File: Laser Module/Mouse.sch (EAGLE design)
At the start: 74 parts, among them Q2 2.5A/30V, U1 RFM69HCW, U10 74AHC1G125, U2 HALL-EFFECTSMD, U3 HALL-EFFECTSMD, U4 HALL-EFFECTSMD, U5 HALL-EFFECTSMD, U6 BQ27441-G1, U7 BQ24075, U8 ATSAMD21G-A, U9 3.3V, Y1 32.768kHz

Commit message: Worked on the laser and dongle schematics Placed the parts on the laser and dongle boards in their rough locations
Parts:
- removed D7: RED, SparkFun-LED:LED-RED0603
- removed F1: 500mA, SparkFun-PowerIC:PTCSMD
- removed L1: FB - 30Ohm, SparkFun-Passives:INDUCTOR0603
- removed Q2: 2.5A/30V, SparkFun-DiscreteSemi:MOSFET-PCHANNELDMG2307L
- removed R19: 10K, SparkFun-Resistors:10KOHM-1/10W-1%(0603)0603
- removed R32: 47K, SparkFun-Resistors:47KOHM1/10W1%(0603)
- removed SJ6: PWR-LED, SparkFun-Passives:JUMPER-PAD-2-NC_BY_TRACENO_SILK
- removed U10: 74AHC1G125, SparkFun-DigitalIC:74AHC1G125
- added ANT: (no value), SparkFun-Connectors:M01PTH_2MM
- added LASER: (no value), SparkFun-Connectors:M021X02_NO_SILK
- added Q1: MOSFET-NCHANNELAO3404A, SparkFun-DiscreteSemi:MOSFET-NCHANNELAO3404A
- added R10, R20, R21, R23, R25, R29: 10k, SparkFun-Resistors:330OHM1/10W1%(0603)
- added R33: 10K, SparkFun-Resistors:10KOHM-1/10W-1%(0603)0603
- added S3, S5, S6, S7, S8, S9: SWITCH-MOMENTARY-2SMD-4, SparkFun-Electromechanical:SWITCH-MOMENTARY-2SMD-4
- JP22: value CORTEX_DEBUGPTH -> CORTEX_DEBUGSMD; device samd21-temp:CORTEX_DEBUGPTH -> SparkFun-Connectors:CORTEX_DEBUGSMD
- R18: value 10K -> 330; device SparkFun-Resistors:10KOHM-1/10W-1%(0603)0603 -> SparkFun-Resistors:330OHM1/10W1%(0603)
- R28: value 330 -> 10k
- S4: value RESET -> SWITCH-MOMENTARY-2SMD-4; device samd21-temp:SWITCH-MOMENTARY-2SMD-4.6X2.8MM -> SparkFun-Electromechanical:SWITCH-MOMENTARY-2SMD-4
- renumbered JP11 to SUPP
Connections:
- removed net A0: U8.PA02(AIN0/DAC)
- removed net A1: U8.PB08(AIN2/SER4:0/TC4:0)
- removed net A2: U8.PB09(AIN3/SER4:1/TC4:1)
- removed net A3: U8.PA04(AIN4/REFB/SER0:0/TC0:0)
- removed net AREF: U8.PA03(AIN1/REFA)
- removed net D0/RXI: U8.PA11(AIN19/SER0:3+)
- removed net D1/TXO: U8.PA10(AIN18/SER0:2+)
- removed net D10/SS: U8.PA18(SER1:2+)
- removed net D11/MOSI: U8.PA16(I2C/SER1:0+)
- removed net D12/MISO: U8.PA19(SER1:3+)
- removed net D13/SCK: U8.PA17(I2C/SER1:1+)
- removed net D2: U8.PA14(XIN/SER2:2+)
- removed net D3: U8.PA09(I2C/AIN17/SER0:1+)
- removed net D4: U8.PA08(I2C/AIN16/SER0:0+)
- removed net D5: U8.PA15(XOUT/SER2:3+)
- removed net D6: U8.PA20(SER5:2+)
- removed net D7: U8.PA21(SER5:3+)
- removed net D8: U8.PA06(AIN6/SER0:2/TC1:0)
- removed net D9: U8.PA07(AIN7/SER0:3/TC1:1)
- removed net EN2: U7.EN2
- removed net N$14: D7.A, R28.1
- removed net N$18: F1.2, Q2.D
- removed net N$20: Q2.G, R32.1, U10.Y
- removed net N$23: D7.C, SJ6.2
- removed net RF_NSS: U1.NSS
- removed net RX_LED: U8.PB03(AIN11/SER5:1)
- removed net SCL: U8.PA23(I2C/SER3:0+)
- removed net SDA: U8.PA22(I2C/SER3:0+)
- removed net TRK_BTN: R5.2, S1.2
- removed net TX_LED: U8.PA27
- new net DWN_BTN: R23.2, S6.1, U8.PA10(AIN18/SER0:2+)
- new net LFT_BTN: R10.2, S3.1, U8.PB09(AIN3/SER4:1/TC4:1)
- new net LFT_MOUSE: R28.2, S8.1, U8.PA12(I2C/SER2:0+)
- new net LSR_BTN: R25.2, S7.1, U8.PA11(AIN19/SER0:3+)
- new net LSR_OUT: R18.2, U8.PA04(AIN4/REFB/SER0:0/TC0:0)
- new net MDL_MOUSE: R5.2, S1.2, U8.PA06(AIN6/SER0:2/TC1:0)
- new net N$6: Q1.G, R18.1
- new net N$8: LASER.2, Q1.D
- new net RF_SS: U1.NSS, U8.PA18(SER1:2+)
- new net RHT_BTN: R21.2, S5.1, U8.PA09(I2C/AIN17/SER0:1+)
- new net RHT_MOUSE: R29.2, S9.1, U8.PA13(I2C/SER2:1+)
- new net UP_BTN: R20.2, S4.1, U8.PA08(I2C/AIN16/SER0:0+)
- net !RESET: no longer S4.2
- net 3.3V: now also S3.2, S4.2, S5.2, S6.2, S7.2, S8.2, S9.2; no longer L1.1, R28.2
- net ANT: now also ANT.1
- net BLU_PWM: now also U8.PA14(XIN/SER2:2+)
- net BMS_SCL: now also U8.PA23(I2C/SER3:0+)
- net BMS_SDA: now also U8.PA22(I2C/SER3:0+)
- net EN1: now also R33.2; no longer R18.2
- net GND: now also Q1.S, R10.1, R20.1, R21.1, R23.1, R25.1, R28.1, R29.1, U7.EN2; no longer R19.2, S4.1, SJ6.1, U10.GND
- net GPOUT: now also U8.PA05(AIN5/SER0:1/TC0:1)
- net GRN_PWM: now also U8.PA20(SER5:2+)
- net HALL_DWN: now also U8.PB02(AIN10/SER5:0)
- net HALL_LFT: now also U8.PB03(AIN11/SER5:1)
- net HALL_RHT: now also U8.PB08(AIN2/SER4:0/TC4:0)
- net HALL_UP: now also U8.PA07(AIN7/SER0:3/TC1:1)
- net N$19: no longer U10./OE, U10.A
- net OUT: now also R33.1; no longer R18.1, R19.1
- net RED_PWM: now also U8.PA15(XOUT/SER2:3+)
- net RF_MISO: now also U8.PA19(SER1:3+)
- net RF_MOSI: now also U8.PA16(I2C/SER1:0+)
- net RF_SCK: now also U8.PA17(I2C/SER1:1+)
- net VDDANA: no longer L1.2
- net VIN: no longer Q2.S, R32.2, U10.VCC
- net V_BATT: now also LASER.1
- net V_USB: no longer F1.1
- net WHT_PWM: now also U8.PA21(SER5:3+)
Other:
- note added: "Buttons"
- note added: "Laser Output"
- note removed: "Charge Current Select"
- note removed: "LEDs!!!"
- note removed: "PA12 is SPI MISO (on SPI header)."
- note removed: "PA13 is DGI GPIO0 (goes to EDBG)."
- note removed: "PA5 is A4"
- note removed: "PB10/11 are MOSI/SCK to SPI header."
- note removed: "PB2 is A5"
- note removed: "PB22/23 are TXD/RXD to the EDBG"
- note removed: "SJ1 enable's disconnecting the Power LED indicator. For power-saving requirements. Default: closed."
- moved on the sheet: C9, D5, D6, JP22, R15, R16, R18, R28, S4

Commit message: Created, placed, and routed a starter board for the Camera Module
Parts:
- ANT: device SparkFun-Connectors:M01PTH_2MM -> SparkFun-Connectors:M01PTH_NO_SILK_YES_STOP
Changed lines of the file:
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@@
 <part name="GND34" library="SparkFun-Aesthetics" deviceset="GND" device=""/>
 <part name="R33" library="SparkFun-Resistors" deviceset="10KOHM-1/10W-1%(0603)" device="0603" value="10K"/>
-<part name="ANT" library="SparkFun-Connectors" deviceset="M01" device="PTH_2MM"/>
+<part name="ANT" library="SparkFun-Connectors" deviceset="M01" device="PTH_NO_SILK_YES_STOP"/>
 <part name="Q1" library="SparkFun-DiscreteSemi" deviceset="MOSFET-NCHANNEL" device="AO3404A"/>
 <part name="GND35" library="SparkFun" deviceset="GND" device=""/>

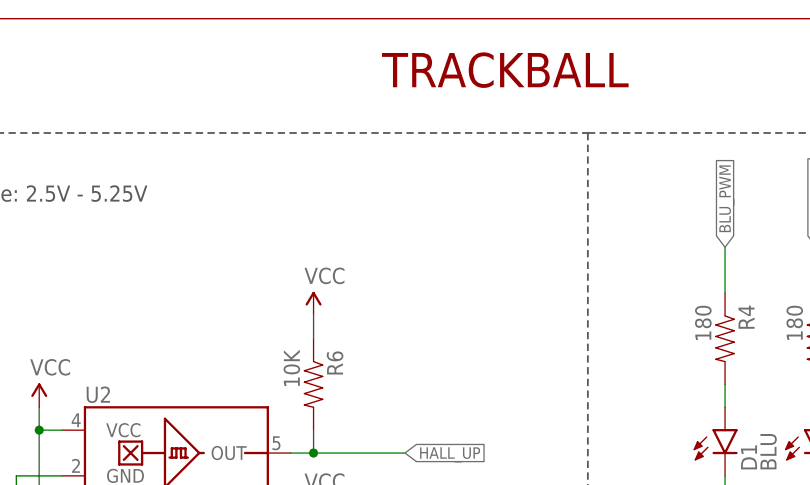
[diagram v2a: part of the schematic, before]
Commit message: Routed the dongle and camera modules
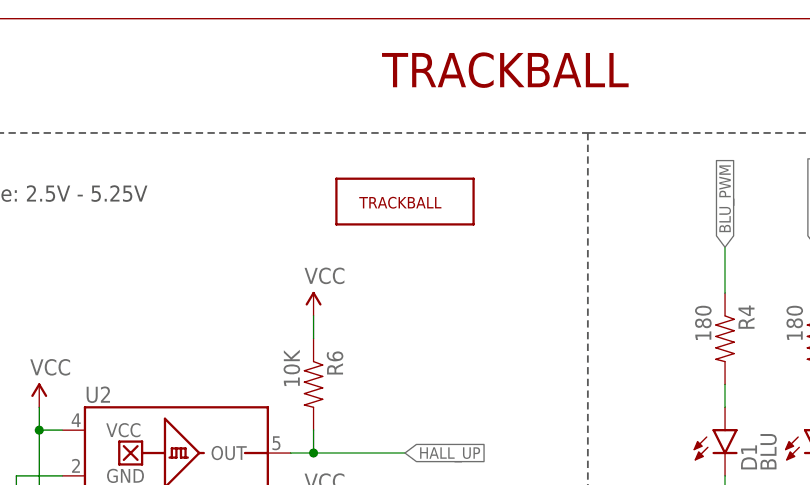
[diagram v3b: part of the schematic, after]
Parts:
- added U$1: TRACKBALLMECH, SparkFun-Electromechanical:TRACKBALLMECH
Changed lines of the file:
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@@
 <part name="LASER" library="SparkFun-Connectors" deviceset="M02" device="1X02_NO_SILK"/>
 <part name="SUPPLY23" library="SparkFun-Aesthetics" deviceset="V_BATT" device=""/>
+<part name="U$1" library="SparkFun-Electromechanical" deviceset="TRACKBALL" device="MECH"/>
 </parts>
 <sheets>
@@
 <instance part="LASER" gate="G$1" x="426.72" y="208.28" rot="R180"/>
 <instance part="SUPPLY23" gate="G$1" x="414.02" y="213.36"/>
+<instance part="U$1" gate="G$1" x="264.16" y="307.34"/>
 </instances>
 <busses>

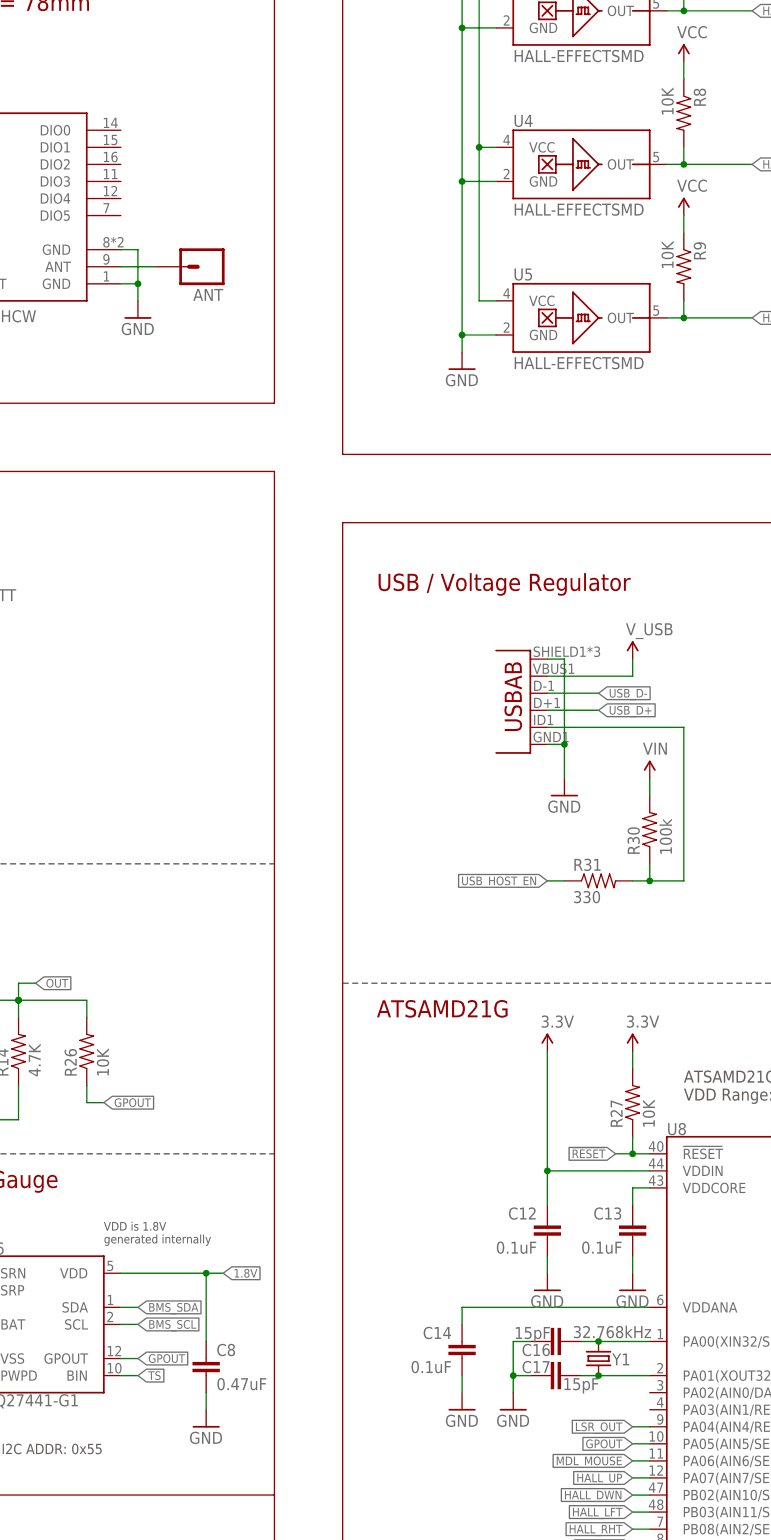
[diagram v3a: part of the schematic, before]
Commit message: Updated the RFM69 library to be closer to C. millis() is the only function hat needs to be updated now.
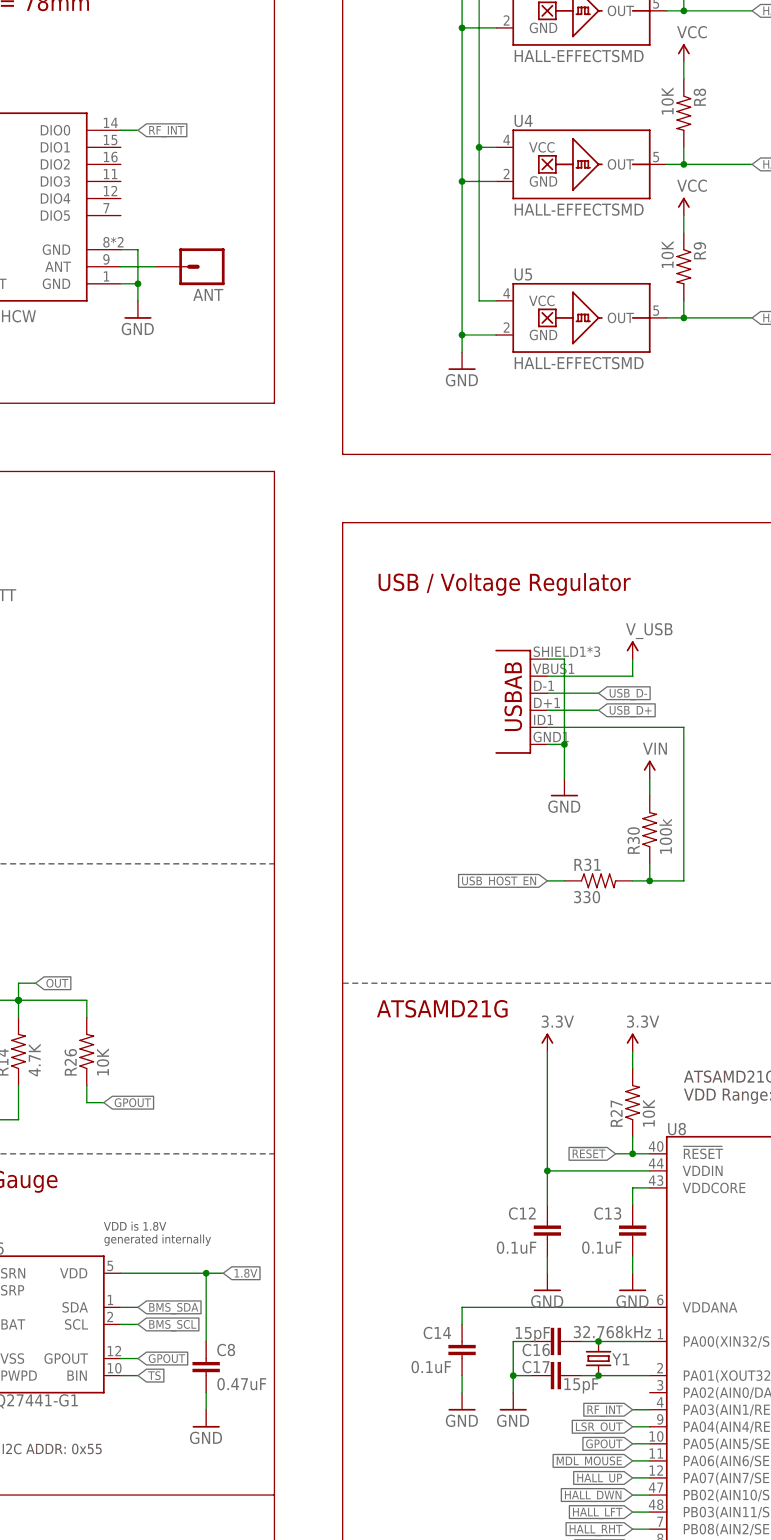
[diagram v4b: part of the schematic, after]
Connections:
- new net RF_INT: U1.DIO0, U8.PA03(AIN1/REFA)
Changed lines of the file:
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@@
+</segment>
+</net>
+<net name="RF_INT" class="0">
+<segment>
+<pinref part="U1" gate="G$1" pin="DIO0"/>
+<wire x1="170.18" y1="238.76" x2="172.72" y2="238.76" width="0.1524" layer="91"/>
+<label x="172.72" y="238.76" size="1.27" layer="95" xref="yes"/>
+</segment>
+<segment>
+<pinref part="U8" gate="G$1" pin="PA03(AIN1/REFA)"/>
+<wire x1="248.92" y1="48.26" x2="246.38" y2="48.26" width="0.1524" layer="91"/>
+<label x="246.38" y="48.26" size="1.27" layer="95" rot="R180" xref="yes"/>
 </segment>
 </net>

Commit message: Started the routing of the laser module board Updated the Dongle Module C project to allow for absolute mouse control
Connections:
- removed net VCC: C3.1, C4.1, C5.1, C6.1, R5.1, R6.1, R7.1, R8.1, R9.1, U2.VCC, U3.VCC, U4.VCC, U5.VCC
- removed net VIN: C18.1, R30.2, U9.EN, U9.IN
- net 3.3V: now also C3.1, C4.1, C5.1, C6.1, R5.1, R6.1, R7.1, R8.1, R9.1, U2.VCC, U3.VCC, U4.VCC, U5.VCC
- net OUT: now also C18.1, R30.2, U9.EN, U9.IN

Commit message: Finished routing the laser module
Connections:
- net BLU_PWM: now also U8.PA08(I2C/AIN16/SER0:0+); no longer U8.PA14(XIN/SER2:2+)
- net DWN_BTN: now also R20.2, S4.1, U8.PA12(I2C/SER2:0+); no longer R23.2, S6.1, U8.PA10(AIN18/SER0:2+)
- net GRN_PWM: now also U8.PA21(SER5:3+); no longer U8.PA20(SER5:2+)
- net HALL_DWN: now also U8.PA09(I2C/AIN17/SER0:1+); no longer U8.PB02(AIN10/SER5:0)
- net HALL_LFT: now also U8.PA10(AIN18/SER0:2+); no longer U8.PB03(AIN11/SER5:1)
- net HALL_RHT: now also U8.PA11(AIN19/SER0:3+); no longer U8.PB08(AIN2/SER4:0/TC4:0)
- net HALL_UP: now also U8.PA06(AIN6/SER0:2/TC1:0); no longer U8.PA07(AIN7/SER0:3/TC1:1)
- net LFT_MOUSE: now also R25.2, S7.1, U8.PB02(AIN10/SER5:0); no longer R28.2, S8.1, U8.PA12(I2C/SER2:0+)
- net LSR_BTN: now also R29.2, S9.1, U8.PB03(AIN11/SER5:1); no longer R25.2, S7.1, U8.PA11(AIN19/SER0:3+)
- net LSR_OUT: now also U8.PB08(AIN2/SER4:0/TC4:0); no longer U8.PA04(AIN4/REFB/SER0:0/TC0:0)
- net MDL_MOUSE: now also U8.PA13(I2C/SER2:1+); no longer U8.PA06(AIN6/SER0:2/TC1:0)
- net RED_PWM: now also U8.PA07(AIN7/SER0:3/TC1:1); no longer U8.PA15(XOUT/SER2:3+)
- net RHT_BTN: now also U8.PA04(AIN4/REFB/SER0:0/TC0:0); no longer U8.PA09(I2C/AIN17/SER0:1+)
- net RHT_MOUSE: now also R28.2, S8.1, U8.PA15(XOUT/SER2:3+); no longer R29.2, S9.1, U8.PA13(I2C/SER2:1+)
- net UP_BTN: now also R23.2, S6.1, U8.PA20(SER5:2+); no longer R20.2, S4.1, U8.PA08(I2C/AIN16/SER0:0+)
- net WHT_PWM: now also U8.PA14(XIN/SER2:2+); no longer U8.PA21(SER5:3+)

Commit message: Finalized all PCBs
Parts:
- C12, C13, C14, C15: device SparkFun-Capacitors:0.1UF-16V(+-10%)(0402) -> SparkFun-Capacitors:CAP0603-CAP
- C16, C17: device samd21-temp:15PF-50V(+-5%)(0402) -> SparkFun-Capacitors:CAP0603-CAP
- D6: value RED -> GREEN
- R1, R4: value 180 -> 91
- R16: value 1K -> 330
- R2: value 180 -> 68
- R3: value 180 -> 75
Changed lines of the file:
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@@
 <part name="GND8" library="SparkFun" deviceset="GND" device=""/>
 <part name="C6" library="SparkFun-Capacitors" deviceset="0.1UF-25V(+80/-20%)(0603)" device="" value="0.1uF"/>
-<part name="R1" library="SparkFun-Resistors" deviceset="180OHM1/10W1%(0603)" device="" value="180"/>
-<part name="R2" library="SparkFun-Resistors" deviceset="180OHM1/10W1%(0603)" device="" value="180"/>
-<part name="R3" library="SparkFun-Resistors" deviceset="180OHM1/10W1%(0603)" device="" value="180"/>
-<part name="R4" library="SparkFun-Resistors" deviceset="180OHM1/10W1%(0603)" device="" value="180"/>
+<part name="R1" library="SparkFun-Resistors" deviceset="180OHM1/10W1%(0603)" device="" value="91"/>
+<part name="R2" library="SparkFun-Resistors" deviceset="180OHM1/10W1%(0603)" device="" value="68"/>
+<part name="R3" library="SparkFun-Resistors" deviceset="180OHM1/10W1%(0603)" device="" value="75"/>
+<part name="R4" library="SparkFun-Resistors" deviceset="180OHM1/10W1%(0603)" device="" value="91"/>
 <part name="GND9" library="SparkFun" deviceset="GND" device=""/>
 <part name="GND10" library="SparkFun" deviceset="GND" device=""/>
@@
 <part name="SUPPLY8" library="SparkFun-Aesthetics" deviceset="V_BATT" device=""/>
 <part name="D5" library="SparkFun-LED" deviceset="LED-BLUE" device="0603" value="BLUE"/>
-<part name="D6" library="SparkFun-LED" deviceset="LED-RED" device="0603" value="RED"/>
+<part name="D6" library="SparkFun-LED" deviceset="LED-RED" device="0603" value="GREEN"/>
 <part name="R15" library="SparkFun-Resistors" deviceset="180OHM1/10W1%(0603)" device="" value="180"/>
-<part name="R16" library="SparkFun-Resistors" deviceset="1KOHM-1/10W-1%(0603)" device="" value="1K"/>
+<part name="R16" library="SparkFun-Resistors" deviceset="1KOHM-1/10W-1%(0603)" device="" value="330"/>
 <part name="C9" library="SparkFun-Capacitors" deviceset="10UF10V10%(0805)" device="" value="10uF"/>
 <part name="GND26" library="SparkFun-Aesthetics" deviceset="GND" device=""/>
@@
 <part name="U8" library="samd21-temp" deviceset="ATSAMD21G" device="-A"/>
 <part name="GND40" library="SparkFun-Aesthetics" deviceset="GND" device=""/>
-<part name="C12" library="SparkFun-Capacitors" deviceset="0.1UF-16V(+-10%)(0402)" device="" value="0.1uF"/>
-<part name="C13" library="SparkFun-Capacitors" deviceset="0.1UF-16V(+-10%)(0402)" device="" value="0.1uF"/>
-<part name="C14" library="SparkFun-Capacitors" deviceset="0.1UF-16V(+-10%)(0402)" device="" value="0.1uF"/>
-<part name="C15" library="SparkFun-Capacitors" deviceset="0.1UF-16V(+-10%)(0402)" device="" value="0.1uF"/>
+<part name="C12" library="SparkFun-Capacitors" deviceset="CAP" device="0603-CAP" value="0.1uF"/>
+<part name="C13" library="SparkFun-Capacitors" deviceset="CAP" device="0603-CAP" value="0.1uF"/>
+<part name="C14" library="SparkFun-Capacitors" deviceset="CAP" device="0603-CAP" value="0.1uF"/>
+<part name="C15" library="SparkFun-Capacitors" deviceset="CAP" device="0603-CAP" value="0.1uF"/>
 <part name="R27" library="SparkFun-Resistors" deviceset="10KOHM-1/10W-1%(0603)" device="0603" value="10K"/>
 <part name="SUPPLY12" library="SparkFun-Aesthetics" deviceset="3.3V" device=""/>
@@
 <part name="GND42" library="SparkFun-Aesthetics" deviceset="GND" device=""/>
 <part name="GND43" library="SparkFun-Aesthetics" deviceset="GND" device=""/>
-<part name="C16" library="samd21-temp" deviceset="15PF-50V(+-5%)(0402)" device="" value="15pF"/>
-<part name="C17" library="samd21-temp" deviceset="15PF-50V(+-5%)(0402)" device="" value="15pF"/>
+<part name="C16" library="SparkFun-Capacitors" deviceset="CAP" device="0603-CAP" value="15pF"/>
+<part name="C17" library="SparkFun-Capacitors" deviceset="CAP" device="0603-CAP" value="15pF"/>
 <part name="GND44" library="SparkFun-Aesthetics" deviceset="GND" device=""/>
 <part name="SUPPLY15" library="SparkFun-Aesthetics" deviceset="3.3V" device=""/>
@@
 <instance part="C16" gate="G$1" x="236.22" y="58.42" smashed="yes" rot="R90">
 <attribute name="NAME" x="234.188" y="58.039" size="1.778" layer="95" rot="R180"/>
-<attribute name="VALUE" x="234.188" y="58.801" size="1.778" layer="96" rot="MR0"/>
 </instance>
 <instance part="C17" gate="G$1" x="233.68" y="53.34" smashed="yes" rot="R270">
 <attribute name="NAME" x="234.188" y="53.721" size="1.778" layer="95" rot="MR0"/>
-<attribute name="VALUE" x="235.966" y="52.959" size="1.778" layer="96" rot="MR180"/>
 </instance>
 <instance part="GND44" gate="1" x="228.6" y="48.26"/>
